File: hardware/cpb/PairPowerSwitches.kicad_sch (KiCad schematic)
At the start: 5 parts, among them Q24 MBT2222ADW1T1, Q25 IRF7306

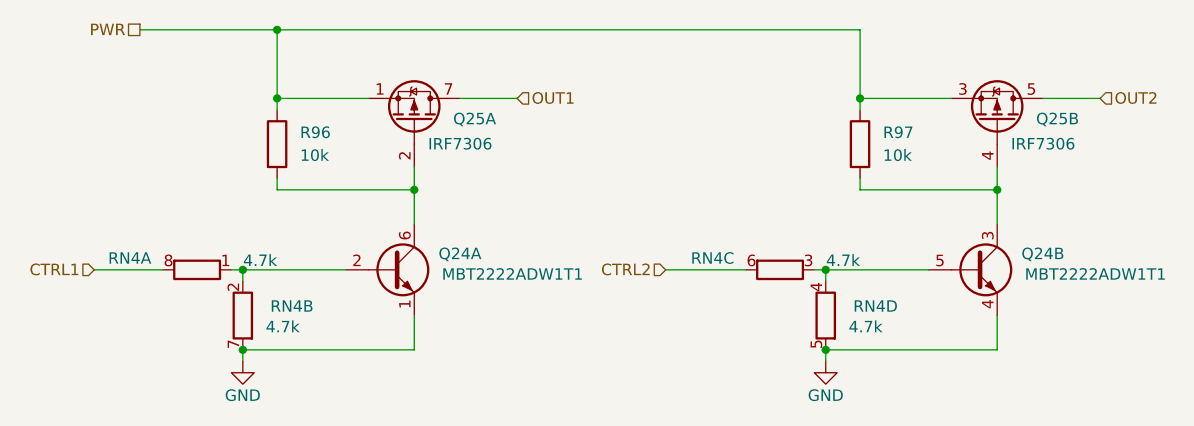
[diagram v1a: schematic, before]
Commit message: hardware/cpb: r96 changed to  3.3k and r46 added
R96 changed resistance from 10k to 3.3k, r46 added from 3.3v to Max22200(1k resistance)
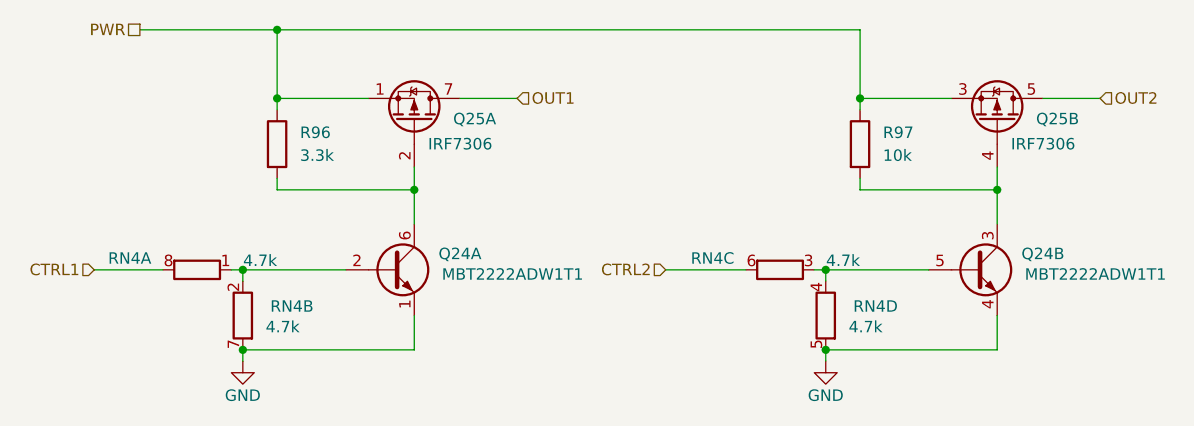
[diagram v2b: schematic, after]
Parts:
- R96: value 10k -> 3.3k; LCSC C844918 -> C108078
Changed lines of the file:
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@@
 			)
 		)
-		(property "Value" "10k"
+		(property "Value" "3.3k"
 			(at 62.23 46.9899 0)
 			(effects
@@
 			)
 		)
-		(property "LCSC" "C844918"
+		(property "LCSC" "C108078"
 			(at 59.69 45.72 0)
 			(effects

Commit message: hardware/cpb: changed from european to american symbols.
RN parts still are european for now. Changed via TextEdit replace all tool. Device:R --> Device:R_US
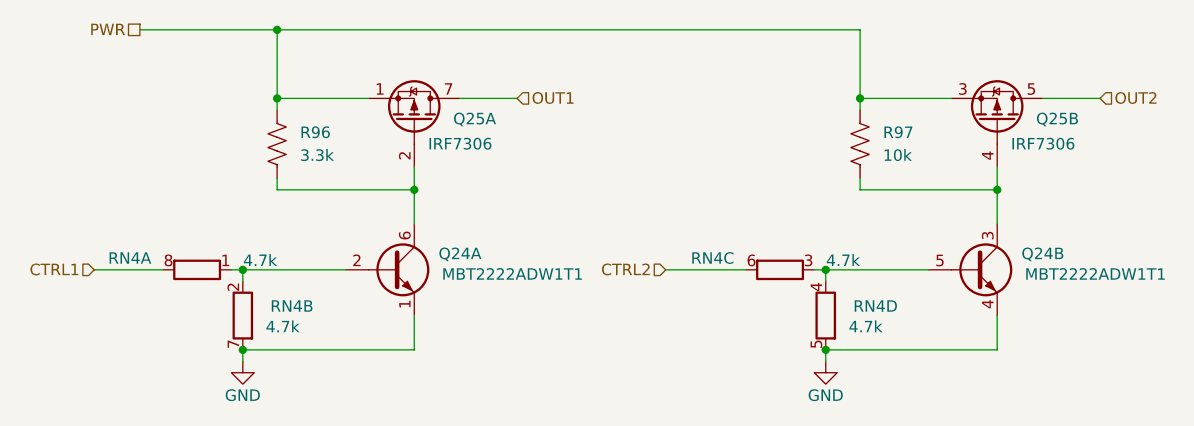
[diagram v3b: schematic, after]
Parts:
- R96, R97: symbol Device:R -> Device:R_US
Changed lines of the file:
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@@
 	)
 	(symbol
-		(lib_id "Device:R")
+		(lib_id "Device:R_US")
 		(at 124.46 45.72 0)
 		(unit 1)
@@
 	)
 	(symbol
-		(lib_id "Device:R")
+		(lib_id "Device:R_US")
 		(at 59.69 45.72 0)
 		(unit 1)

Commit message: hardware/cpb: finished revisions
did all things specified on Errata file for cpb;
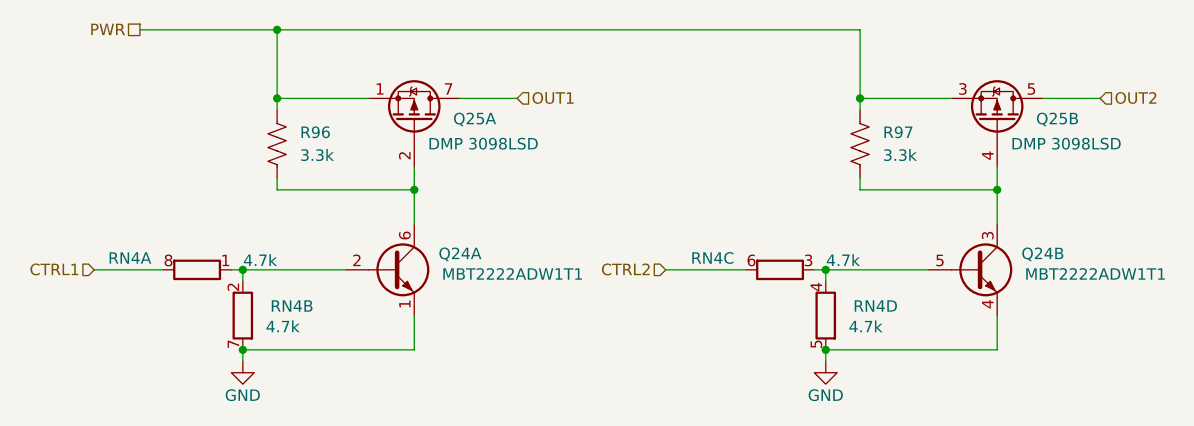
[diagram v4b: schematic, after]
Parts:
- Q25: value IRF7306 -> DMP 3098LSD; LCSC C537809 -> C531177
- R97: value 10k -> 3.3k; LCSC C844918 -> C108078
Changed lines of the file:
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@@
 			)
 		)
-		(property "Value" "IRF7306"
+		(property "Value" "DMP 3098LSD"
 			(at 141.224 45.72 90)
 			(effects
@@
 			)
 		)
-		(property "LCSC" "C537809 "
+		(property "LCSC" "C531177"
 			(at 139.7 43.18 0)
 			(effects
@@
 			)
 		)
-		(property "Value" "10k"
+		(property "Value" "3.3k"
 			(at 127 46.9899 0)
 			(effects
@@
 			)
 		)
-		(property "LCSC" "C844918"
+		(property "LCSC" "C108078"
 			(at 124.46 45.72 0)
 			(effects
@@
 			)
 		)
-		(property "Value" "IRF7306"
+		(property "Value" "DMP 3098LSD"
 			(at 76.454 45.72 90)
 			(effects
@@
 			)
 		)
-		(property "LCSC" "C537809 "
+		(property "LCSC" "C531177"
 			(at 74.93 43.18 0)
 			(effects

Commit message: hardware/cpb: changed labels, spread out components
changed vm labels, spread out somponents on Four Full Bridges sch;
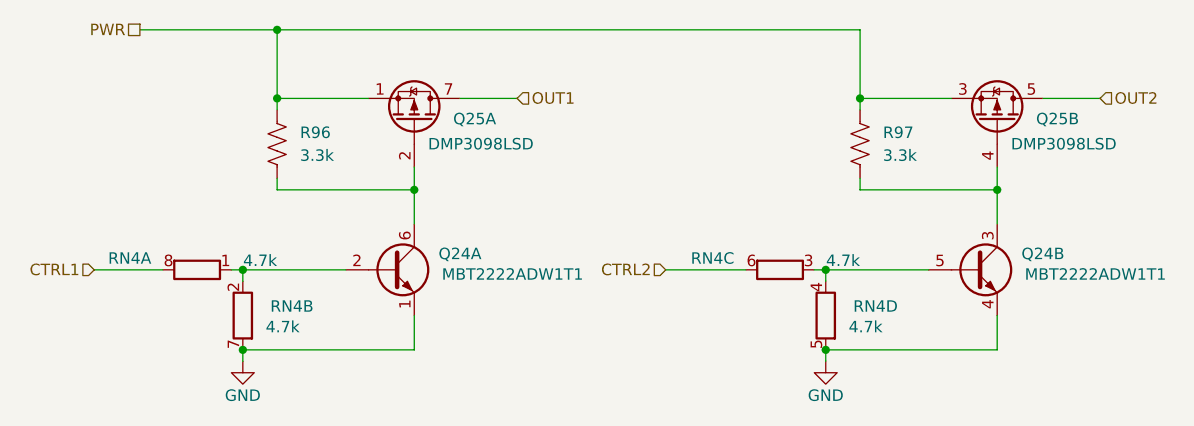
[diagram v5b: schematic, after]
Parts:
- Q25: value DMP 3098LSD -> DMP3098LSD
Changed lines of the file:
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@@
 			)
 		)
-		(property "Value" "DMP 3098LSD"
+		(property "Value" "DMP3098LSD"
 			(at 141.224 45.72 90)
 			(effects
@@
 			)
 		)
-		(property "Value" "DMP 3098LSD"
+		(property "Value" "DMP3098LSD"
 			(at 76.454 45.72 90)
 			(effects
